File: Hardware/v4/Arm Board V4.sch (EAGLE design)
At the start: 60 parts, among them IC3 L6206D, P1 STELLARIS-LAUNCHPADSTELLARIS-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, U1 SN74LS241DW, U2 XBEE-1B3, U3 LSM9DS0

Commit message: reworking arm board
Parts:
- removed C10: 330uF, SparkFun-Capacitors:CAP_POLE
- removed C11, C20: 1.0uF, SparkFun-Capacitors:1.0UF50V10%(1206)
- removed C2: 5.6nF, SparkFun-Passives:CAP1206
- removed C21, C22, C23, C24, C38: 4.7uF, SparkFun-Capacitors:CAP1206
- removed C36: 10uF, SparkFun-Capacitors:10UF-16V-10%(TANT)
- removed C37: 1uF, SparkFun-Capacitors:CAP1206
- removed C39: .22uF, SparkFun-Capacitors:CAP1206
- removed C4: 220nF, SparkFun-Passives:CAP1206
- removed C9: 10nF, SparkFun-Passives:CAP1206
- removed D1, D2: 1N4148, SparkFun-DiscreteSemi:DIODE1N4148
- removed IC3: L6206D, L6206D:L6206D
- removed JP4: (no value), SparkFun-Connectors:M04PTH
- removed JP7: (no value), SparkFun-Connectors:M03PTH
- removed R1: 17.2k, SparkFun-Passives:RESISTOR1206
- removed R15: 100, SparkFun-Resistors:RESISTOR1206
- removed R30, R31, R32, R33, R34, R35: 10k, SparkFun-Resistors:RESISTOR1206
- removed R8: 100k, SparkFun-Resistors:RESISTOR1206
- removed U$2: Q_PTN78020, MRDT-2014-All:Q_PTN78020
- removed U$5: 691321100003, MRDT-2015-PowerBoard:691321100003
- removed U$6: H_WR-TBL_3210002VERT, MRDT-2015-PowerBoard:H_WR-TBL_3210002VERT
- removed U3: LSM9DS0, SparkFun-DigitalIC:LSM9DS0
- added U$1: TORXIS_BREAKOUT, MRDT-RoboticArm:TORXIS_BREAKOUT
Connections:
- removed net A1: IC3.OUT1_A, U$6.L
- removed net A2: IC3.OUT2_A, U$6.R
- removed net CS_G: R30.1, U3.CS(G)
- removed net CS_XM: R31.1, U3.CS(XM)
- removed net DEN_G: U3.DEN(G)
- removed net DRDY_G: U3.DRDY(G)
- removed net EN_A: P1.PD2, R8.2
- removed net IN1_A: IC3.IN1_A, P1.PD3
- removed net N$10: C39.1, U3.SETP
- removed net N$17: D1.A, D2.C, R15.2
- removed net N$18: C9.2, R15.1
- removed net N$19: C9.1, IC3.VCP
- removed net OCD_A: C2.2, IC3.EN_A, IC3.OCD_A, R8.1
- removed net SDO_G: R32.1, U3.SDO(G)
- removed net SDO_XM: R33.1, U3.SDO(XM)
- removed net VBOOT: C4.2, D1.C, IC3.VBOOT
- new net N$21: U$1.A
- new net N$22: U$1.B
- net +12V: now also U$1.VIN; no longer C4.1, D2.A, IC3.VS_A, IC3.VS_B, U$5.L
- net +3V3: no longer C36.+, C37.1, JP4.2, JP7.2, R30.2, R31.2, R32.2, R33.2, R34.2, R35.2, U3.VDD, U3.VDD_IO
- net 14.8V: no longer C10.+, C11.1, U$2.VOUT
- net GND: now also U$1.GND@1, U$1.GND@4; no longer C10.-, C11.2, C2.1, C20.2, C21.2, C22.2, C23.2, C24.2, C36.-, C37.2, C38.2, IC3.PROGCL_A, IC3.PROGCL_B, IC3.SENSE_A, IC3.SENSE_B, JP4.1, JP7.1, R1.1, U$2.GND, U$2.GND1, U$5.C, U3.GND
- net IN2_A: no longer IC3.IN2_A
- net INT1_XM: no longer U3.INT1(XM)
- net INT2_XM: no longer U3.INT2(XM)
- net INT_G: no longer U3.INT(G)
- net LA_ENC: no longer JP7.3
- net N$11: now also U$1.GND@2; no longer C39.2, U3.SETC
- net N$12: now also U$1.FB; no longer C38.1, U3.C1
- net N$9: now also U$1.+5V@1; no longer R1.2, U$2.ADJUST
- net RX_7: now also U$1.RX
- net SCL: no longer JP4.4, R34.1, U3.SCL
- net SDA: no longer JP4.3, R35.1, U3.SDA
- net VIN: no longer C20.1, C21.1, C22.1, C23.1, C24.1, U$2.VIN, U$5.R
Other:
- note added: "+12V"
- note removed: "0 1"
- note removed: "0x1E 0x1D"
- note removed: "0x6A 0x6B"
- note removed: "Close these jumpers to hard-set I2C mode. Gyro Address = 0x6B Accel/Mag Address = 0x1D"
- note removed: "G Addr."
- note removed: "SDA/SCL Pull-up resistors"
- note removed: "SDOG/XM"
- note removed: "XM Addr."

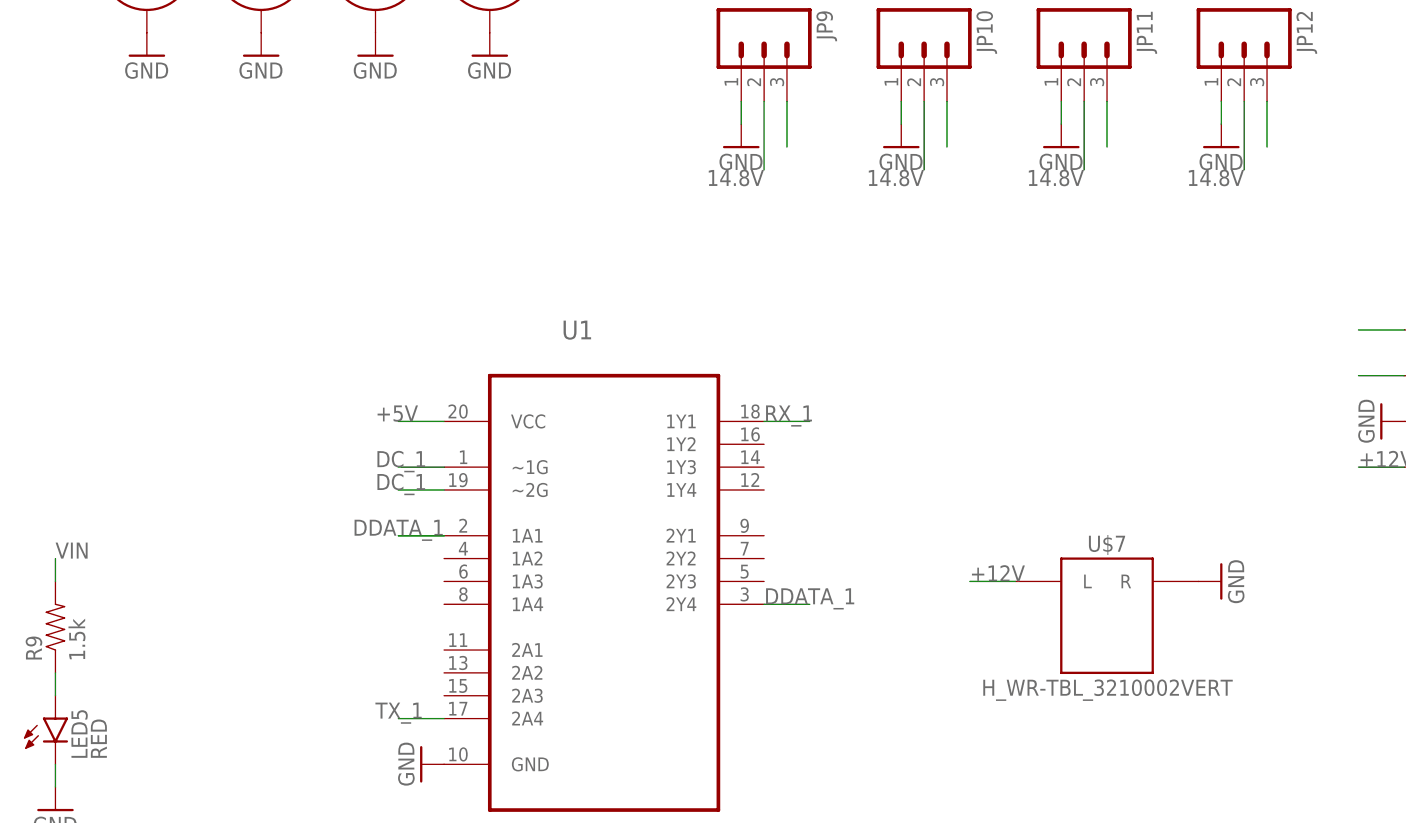
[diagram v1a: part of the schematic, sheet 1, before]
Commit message: reworking arm board
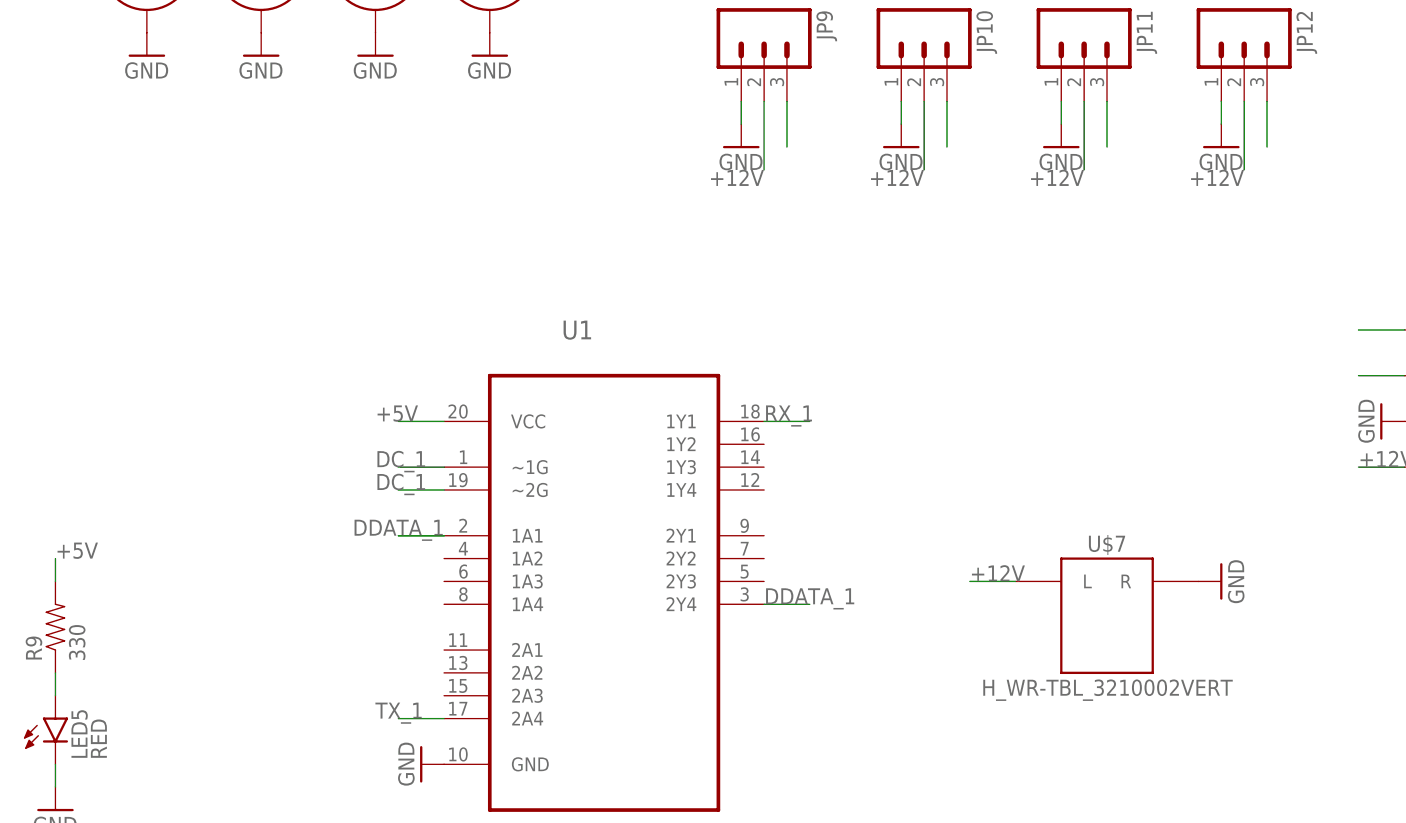
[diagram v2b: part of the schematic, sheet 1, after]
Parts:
- R9: value 1.5k -> 330
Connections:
- removed net 14.8V: JP10.2, JP11.2, JP12.2, JP9.2
- removed net VIN: R9.2
- net +12V: now also JP10.2, JP11.2, JP12.2, JP9.2
- net +5V: now also R9.2
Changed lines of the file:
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@@
 <part name="GND18" library="SparkFun-Aesthetics" deviceset="GND" device=""/>
 <part name="U$4" library="MAX3077" deviceset="MAX3077" device=""/>
-<part name="R9" library="SparkFun-Passives" deviceset="RESISTOR" device="1206" value="1.5k"/>
+<part name="R9" library="SparkFun-Passives" deviceset="RESISTOR" device="1206" value="330"/>
 <part name="LED5" library="SparkFun-LED" deviceset="LED-RED" device="0603" value="RED"/>
 <part name="GND30" library="SparkFun" deviceset="GND" device=""/>
@@
 <wire x1="165.1" y1="2.54" x2="160.02" y2="2.54" width="0.1524" layer="91"/>
 </segment>
-</net>
-<net name="+5V" class="0">
-<segment>
-<pinref part="U1" gate="A" pin="VCC"/>
-<wire x1="58.42" y1="7.62" x2="53.34" y2="7.62" width="0.1524" layer="91"/>
-<label x="50.8" y="7.62" size="1.778" layer="95"/>
-</segment>
-<segment>
-<wire x1="226.06" y1="-25.4" x2="226.06" y2="-33.02" width="0.1524" layer="91"/>
-<pinref part="JP1" gate="G$1" pin="3"/>
-</segment>
-</net>
-<net name="14.8V" class="0">
 <segment>
 <pinref part="JP9" gate="G$1" pin="2"/>
@@
 </segment>
 </net>
-<net name="VIN" class="0">
+<net name="+5V" class="0">
+<segment>
+<pinref part="U1" gate="A" pin="VCC"/>
+<wire x1="58.42" y1="7.62" x2="53.34" y2="7.62" width="0.1524" layer="91"/>
+<label x="50.8" y="7.62" size="1.778" layer="95"/>
+</segment>
+<segment>
+<wire x1="226.06" y1="-25.4" x2="226.06" y2="-33.02" width="0.1524" layer="91"/>
+<pinref part="JP1" gate="G$1" pin="3"/>
+</segment>
 <segment>
 <wire x1="15.24" y1="-7.62" x2="15.24" y2="-10.16" width="0.1524" layer="91"/>

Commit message: still reworking arm board
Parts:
- removed LED5: RED, SparkFun-LED:LED-RED0603
- removed R9: 330, SparkFun-Passives:RESISTOR1206
- added D1: RED, SparkFun-LED:LED-RED0603
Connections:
- removed net N$14: LED5.A, R9.1
- new net DDATA_OUT: D1.A, U1.1A1, U1.2Y4
- net +5V: no longer R9.2
- net DDATA_1: now also D1.C; no longer U1.1A1, U1.2Y4
- net GND: no longer LED5.C
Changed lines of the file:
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@@
 <part name="GND18" library="SparkFun-Aesthetics" deviceset="GND" device=""/>
 <part name="U$4" library="MAX3077" deviceset="MAX3077" device=""/>
-<part name="R9" library="SparkFun-Passives" deviceset="RESISTOR" device="1206" value="330"/>
-<part name="LED5" library="SparkFun-LED" deviceset="LED-RED" device="0603" value="RED"/>
-<part name="GND30" library="SparkFun" deviceset="GND" device=""/>
 <part name="S1" library="SparkFun-Electromechanical" deviceset="STANDOFF_ELECTRICAL" device=""/>
 <part name="S2" library="SparkFun-Electromechanical" deviceset="STANDOFF_ELECTRICAL" device=""/>
@@
 <part name="GND3" library="SparkFun-Aesthetics" deviceset="GND" device=""/>
 <part name="GND10" library="SparkFun-Aesthetics" deviceset="GND" device=""/>
+<part name="D1" library="SparkFun-LED" deviceset="LED-RED" device="0603" value="RED"/>
 </parts>
 <sheets>
@@
 <instance part="U1" gate="A" x="76.2" y="-7.62"/>
 <instance part="GND18" gate="1" x="55.88" y="-30.48" rot="R270"/>
-<instance part="R9" gate="G$1" x="15.24" y="-15.24" rot="R90"/>
-<instance part="LED5" gate="G$1" x="15.24" y="-25.4"/>
-<instance part="GND30" gate="1" x="15.24" y="-35.56"/>
 <instance part="S1" gate="G$1" x="25.4" y="58.42" rot="R270"/>
 <instance part="S2" gate="G$1" x="38.1" y="58.42" rot="R270"/>
@@
 <instance part="GND3" gate="1" x="198.12" y="17.78" rot="R90"/>
 <instance part="GND10" gate="1" x="162.56" y="7.62" rot="R270"/>
+<instance part="D1" gate="G$1" x="99.06" y="-12.7" rot="R90"/>
 </instances>
 <busses>
@@
 </segment>
 <segment>
-<wire x1="15.24" y1="-30.48" x2="15.24" y2="-33.02" width="0.1524" layer="91"/>
-<pinref part="LED5" gate="G$1" pin="C"/>
-<pinref part="GND30" gate="1" pin="GND"/>
-</segment>
-<segment>
 <pinref part="U$7" gate="G$1" pin="R"/>
 <pinref part="GND9" gate="1" pin="GND"/>
@@
 <pinref part="JP1" gate="G$1" pin="3"/>
 </segment>
-<segment>
-<wire x1="15.24" y1="-7.62" x2="15.24" y2="-10.16" width="0.1524" layer="91"/>
-<pinref part="R9" gate="G$1" pin="2"/>
-<label x="15.24" y="-7.62" size="1.778" layer="95"/>
-</segment>
 </net>
 <net name="DC_1" class="0">
@@
 </net>
 <net name="DDATA_1" class="0">
+<segment>
+<pinref part="JP10" gate="G$1" pin="3"/>
+<wire x1="114.3" y1="43.18" x2="114.3" y2="38.1" width="0.1524" layer="91"/>
+</segment>
+<segment>
+<pinref part="JP11" gate="G$1" pin="3"/>
+<wire x1="132.08" y1="43.18" x2="132.08" y2="38.1" width="0.1524" layer="91"/>
+</segment>
+<segment>
+<pinref part="JP12" gate="G$1" pin="3"/>
+<wire x1="149.86" y1="43.18" x2="149.86" y2="38.1" width="0.1524" layer="91"/>
+</segment>
+<segment>
+<pinref part="JP9" gate="G$1" pin="3"/>
+<wire x1="96.52" y1="43.18" x2="96.52" y2="40.64" width="0.1524" layer="91"/>
+</segment>
+<segment>
+<pinref part="D1" gate="G$1" pin="C"/>
+<wire x1="104.14" y1="-12.7" x2="106.68" y2="-12.7" width="0.1524" layer="91"/>
+<label x="104.14" y="-12.7" size="1.778" layer="95"/>
+</segment>
+</net>
+<net name="RX_1" class="0">
+<segment>
+<pinref part="U1" gate="A" pin="1Y1"/>
+<wire x1="93.98" y1="7.62" x2="99.06" y2="7.62" width="0.1524" layer="91"/>
+<label x="93.98" y="7.62" size="1.778" layer="95"/>
+</segment>
+</net>
+<net name="TX_1" class="0">
+<segment>
+<pinref part="U1" gate="A" pin="2A4"/>
+<wire x1="58.42" y1="-25.4" x2="53.34" y2="-25.4" width="0.1524" layer="91"/>
+<label x="50.8" y="-25.4" size="1.778" layer="95"/>
+</segment>
+</net>
+<net name="TX_3" class="0">
+<segment>
+<pinref part="JP1" gate="G$1" pin="1"/>
+<wire x1="220.98" y1="-25.4" x2="220.98" y2="-33.02" width="0.1524" layer="91"/>
+</segment>
+</net>
+<net name="RX_3" class="0">
+<segment>
+<pinref part="JP1" gate="G$1" pin="2"/>
+<wire x1="223.52" y1="-25.4" x2="223.52" y2="-33.02" width="0.1524" layer="91"/>
+</segment>
+</net>
+<net name="N$9" class="0">
+<segment>
+<pinref part="U$1" gate="G$1" pin="+5V@1"/>
+<wire x1="177.8" y1="25.4" x2="177.8" y2="30.48" width="0.1524" layer="91"/>
+</segment>
+</net>
+<net name="N$11" class="0">
+<segment>
+<pinref part="U$1" gate="G$1" pin="GND@2"/>
+<wire x1="175.26" y1="25.4" x2="175.26" y2="30.48" width="0.1524" layer="91"/>
+</segment>
+</net>
+<net name="N$12" class="0">
+<segment>
+<pinref part="U$1" gate="G$1" pin="FB"/>
+<wire x1="180.34" y1="25.4" x2="180.34" y2="30.48" width="0.1524" layer="91"/>
+</segment>
+</net>
+<net name="RX_7" class="0">
+<segment>
+<pinref part="U$1" gate="G$1" pin="RX"/>
+<wire x1="195.58" y1="12.7" x2="200.66" y2="12.7" width="0.1524" layer="91"/>
+</segment>
+</net>
+<net name="N$21" class="0">
+<segment>
+<pinref part="U$1" gate="G$1" pin="A"/>
+<wire x1="165.1" y1="12.7" x2="160.02" y2="12.7" width="0.1524" layer="91"/>
+</segment>
+</net>
+<net name="N$22" class="0">
+<segment>
+<pinref part="U$1" gate="G$1" pin="B"/>
+<wire x1="165.1" y1="17.78" x2="160.02" y2="17.78" width="0.1524" layer="91"/>
+</segment>
+</net>
+<net name="DDATA_OUT" class="0">
+<segment>
+<pinref part="U1" gate="A" pin="2Y4"/>
+<pinref part="D1" gate="G$1" pin="A"/>
+<wire x1="96.52" y1="-12.7" x2="93.98" y2="-12.7" width="0.1524" layer="91"/>
+<label x="83.82" y="-15.24" size="1.778" layer="95"/>
+</segment>
 <segment>
 <pinref part="U1" gate="A" pin="1A1"/>
@@
 <wire x1="58.42" y1="-5.08" x2="53.34" y2="-5.08" width="0.1524" layer="91"/>
 </segment>
-<segment>
-<pinref part="U1" gate="A" pin="2Y4"/>
-<wire x1="93.98" y1="-12.7" x2="99.06" y2="-12.7" width="0.1524" layer="91"/>
-<label x="93.98" y="-12.7" size="1.778" layer="95"/>
-</segment>
-<segment>
-<pinref part="JP9" gate="G$1" pin="3"/>
-<wire x1="96.52" y1="43.18" x2="96.52" y2="38.1" width="0.1524" layer="91"/>
-</segment>
-<segment>
-<pinref part="JP10" gate="G$1" pin="3"/>
-<wire x1="114.3" y1="43.18" x2="114.3" y2="38.1" width="0.1524" layer="91"/>
-</segment>
-<segment>
-<pinref part="JP11" gate="G$1" pin="3"/>
-<wire x1="132.08" y1="43.18" x2="132.08" y2="38.1" width="0.1524" layer="91"/>
-</segment>
-<segment>
-<pinref part="JP12" gate="G$1" pin="3"/>
-<wire x1="149.86" y1="43.18" x2="149.86" y2="38.1" width="0.1524" layer="91"/>
-</segment>
-</net>
-<net name="RX_1" class="0">
-<segment>
-<pinref part="U1" gate="A" pin="1Y1"/>
-<wire x1="93.98" y1="7.62" x2="99.06" y2="7.62" width="0.1524" layer="91"/>
-<label x="93.98" y="7.62" size="1.778" layer="95"/>
-</segment>
-</net>
-<net name="TX_1" class="0">
-<segment>
-<pinref part="U1" gate="A" pin="2A4"/>
-<wire x1="58.42" y1="-25.4" x2="53.34" y2="-25.4" width="0.1524" layer="91"/>
-<label x="50.8" y="-25.4" size="1.778" layer="95"/>
-</segment>
-</net>
-<net name="N$14" class="0">
-<segment>
-<wire x1="15.24" y1="-22.86" x2="15.24" y2="-20.32" width="0.1524" layer="91"/>
-<pinref part="R9" gate="G$1" pin="1"/>
-<pinref part="LED5" gate="G$1" pin="A"/>
-</segment>
-</net>
-<net name="TX_3" class="0">
-<segment>
-<pinref part="JP1" gate="G$1" pin="1"/>
-<wire x1="220.98" y1="-25.4" x2="220.98" y2="-33.02" width="0.1524" layer="91"/>
-</segment>
-</net>
-<net name="RX_3" class="0">
-<segment>
-<pinref part="JP1" gate="G$1" pin="2"/>
-<wire x1="223.52" y1="-25.4" x2="223.52" y2="-33.02" width="0.1524" layer="91"/>
-</segment>
-</net>
-<net name="N$9" class="0">
-<segment>
-<pinref part="U$1" gate="G$1" pin="+5V@1"/>
-<wire x1="177.8" y1="25.4" x2="177.8" y2="30.48" width="0.1524" layer="91"/>
-</segment>
-</net>
-<net name="N$11" class="0">
-<segment>
-<pinref part="U$1" gate="G$1" pin="GND@2"/>
-<wire x1="175.26" y1="25.4" x2="175.26" y2="30.48" width="0.1524" layer="91"/>
-</segment>
-</net>
-<net name="N$12" class="0">
-<segment>
-<pinref part="U$1" gate="G$1" pin="FB"/>
-<wire x1="180.34" y1="25.4" x2="180.34" y2="30.48" width="0.1524" layer="91"/>
-</segment>
-</net>
-<net name="RX_7" class="0">
-<segment>
-<pinref part="U$1" gate="G$1" pin="RX"/>
-<wire x1="195.58" y1="12.7" x2="200.66" y2="12.7" width="0.1524" layer="91"/>
-</segment>
-</net>
-<net name="N$21" class="0">
-<segment>
-<pinref part="U$1" gate="G$1" pin="A"/>
-<wire x1="165.1" y1="12.7" x2="160.02" y2="12.7" width="0.1524" layer="91"/>
-</segment>
-</net>
-<net name="N$22" class="0">
-<segment>
-<pinref part="U$1" gate="G$1" pin="B"/>
-<wire x1="165.1" y1="17.78" x2="160.02" y2="17.78" width="0.1524" layer="91"/>
-</segment>
-</net>
+</net>
